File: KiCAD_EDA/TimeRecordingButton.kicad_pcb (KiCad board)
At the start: 2 copper layers, 15 x 15 mm, 9 parts, among them J1 USB Micro, J2 Battery, J3 Debug, SW1 SW_Push, U2 PIC16F18114-I/SN

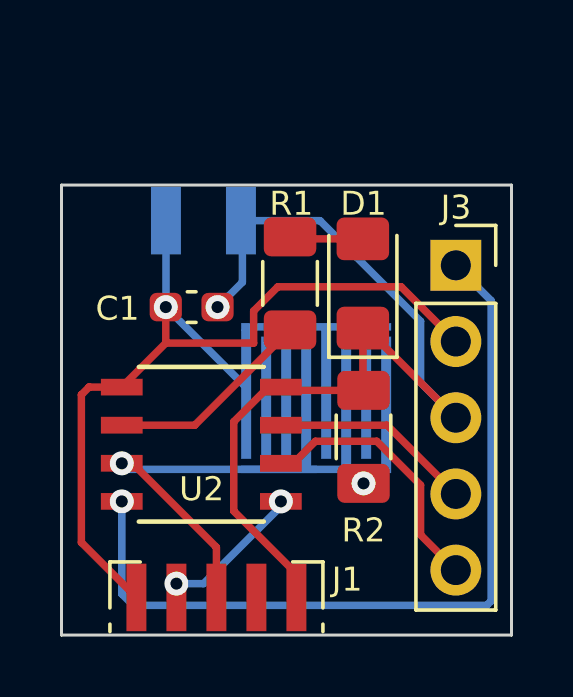
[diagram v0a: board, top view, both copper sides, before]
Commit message: KiCAD v2 and removing backup folders.
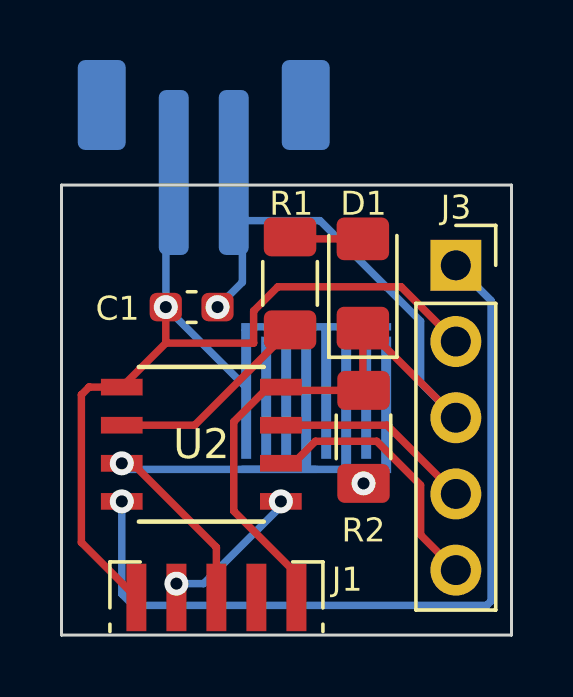
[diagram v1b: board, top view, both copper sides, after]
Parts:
- J2: footprint CustomFootprints:JST_XH_B2B-XH-A_1x02_P2.50mm_SideMount_B -> Connector_JST:JST_PH_B2B-PH-SM4-TB_1x02-1MP_P2.00mm_Vertical; moved to B.Cu
- moved J2 2.45 mm to (104.4, 101.1), turned to 180 degrees
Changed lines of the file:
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@@
     (property "ki_keywords" "PIC16F18114-I/SN")
     (attr smd)
-    (fp_text reference "U2" (at 0.008701 1.495461 unlocked) (layer "F.SilkS")
-        (effects (font (size 0.8 0.8) (thickness 0.12)))
+    (fp_text reference "U2" (at 0 0 unlocked) (layer "F.SilkS")
+        (effects (font (size 1 1) (thickness 0.15)))
     )
     (fp_text value "PIC16F18114-I/SN" (at 0 0 unlocked) (layer "F.Fab")
         (effects (font (size 1 1) (thickness 0.15)))
     )
+    (fp_text user "${REFERENCE}" (at 0 0 unlocked) (layer "F.Fab")
+        (effects (font (size 1 1) (thickness 0.15)))
+    )
+    (fp_text user "*" (at -1.5748 -2.3749) (layer "F.Fab")
+        (effects (font (size 1 1) (thickness 0.15)))
+    )
     (fp_text user "*" (at -1.5748 -2.3749 unlocked) (layer "F.Fab")
-        (effects (font (size 1 1) (thickness 0.15)))
-    )
-    (fp_text user "${REFERENCE}" (at 0 0 unlocked) (layer "F.Fab")
-        (effects (font (size 1 1) (thickness 0.15)))
-    )
-    (fp_text user "*" (at -1.5748 -2.3749) (layer "F.Fab")
         (effects (font (size 1 1) (thickness 0.15)))
     )
@@
     )
   )
-  (footprint "CustomFootprints:JST_XH_B2B-XH-A_1x02_P2.50mm_SideMount_B" (layer "F.Cu")
-    (at 103.150284 103.205284)
-    (descr "JST XH series connector, B2B-XH-A (http://www.jst-mfg.com/product/pdf/eng/eXH.pdf), generated with kicad-footprint-generator")
-    (tags "connector JST XH vertical")
-    (property "Sheetfile" "TimeRecordingButton.kicad_sch")
-    (property "Sheetname" "")
-    (property "ki_description" "Generic connector, single row, 01x02, script generated (kicad-library-utils/schlib/autogen/connector/)")
-    (property "ki_keywords" "connector")
-    (attr through_hole)
-    (fp_text reference "J2" (at -1.952554 0.834925) (layer "B.SilkS")
-        (effects (font (size 0.8 0.8) (thickness 0.12)) (justify mirror))
-    )
-    (fp_text value "Battery" (at 1.264124 -3.589534) (layer "B.Fab")
-        (effects (font (size 1 1) (thickness 0.15)))
-    )
-    (fp_text user "PCB Edge" (at 1.778593 -1.414064 180) (layer "Dwgs.User")
-        (effects (font (size 0.4 0.4) (thickness 0.04)))
-    )
-    (fp_text user "${REFERENCE}" (at 1.25 0) (layer "B.Fab")
-        (effects (font (size 1 1) (thickness 0.15)))
-    )
-    (fp_line (start -2.8 0.25) (end -2.8 1.5)
-      (stroke (width 0.12) (type solid)) (layer "B.SilkS"))
-    (fp_line (start -2.8 1.5) (end -1.55 1.5)
-      (stroke (width 0.12) (type solid)) (layer "B.SilkS"))
-    (fp_line (start -2.95 -2.85) (end -2.95 1.625)
-      (stroke (width 0.05) (type solid)) (layer "B.CrtYd"))
-    (fp_line (start -2.95 1.625) (end 5.45 1.625)
-      (stroke (width 0.05) (type solid)) (layer "B.CrtYd"))
-    (fp_line (start 5.45 -2.85) (end -2.95 -2.85)
-      (stroke (width 0.05) (type solid)) (layer "B.CrtYd"))
-    (fp_line (start 5.45 1.625) (end 5.45 -2.85)
-      (stroke (width 0.05) (type solid)) (layer "B.CrtYd"))
-    (fp_line (start -2.45 -2.35) (end -2.45 -1.125)
-      (stroke (width 0.1) (type solid)) (layer "B.Fab"))
-    (fp_line (start -2.45 -1.125) (end 4.95 -1.125)
-      (stroke (width 0.1) (type solid)) (layer "B.Fab"))
-    (fp_line (start -0.625 -2.35) (end 0 -1.35)
-      (stroke (width 0.1) (type solid)) (layer "B.Fab"))
-    (fp_line (start 0 -1.35) (end 0.625 -2.35)
-      (stroke (width 0.1) (type solid)) (layer "B.Fab"))
-    (fp_line (start 4.95 -2.35) (end -2.45 -2.35)
-      (stroke (width 0.1) (type solid)) (layer "B.Fab"))
-    (fp_line (start 4.95 -1.125) (end 4.95 -2.35)
-      (stroke (width 0.1) (type solid)) (layer "B.Fab"))
-    (pad "1" smd rect (at 0 0) (size 1 2.25) (layers "B.Cu" "B.Paste" "B.Mask")
-      (net 1 "Net-(J1-VBUS)") (pinfunction "Pin_1") (pintype "passive"))
-    (pad "2" smd rect (at 2.5 0) (size 1 2.25) (layers "B.Cu" "B.Paste" "B.Mask")
-      (net 2 "Net-(D1-K)") (pinfunction "Pin_2") (pintype "passive"))
-    (model "${KICAD6_3DMODEL_DIR}/Connector_JST.3dshapes/JST_XH_B2B-XH-A_1x02_P2.50mm_Vertical.wrl"
-      (offset (xyz 0 0 0))
-      (scale (xyz 1 1 1))
-      (rotate (xyz 0 0 0))
-    )
-  )
   (footprint "Connector_PinSocket_2.54mm:PinSocket_1x05_P2.54mm_Vertical" (layer "F.Cu")
     (at 112.812304 104.694022)
@@
       (offset (xyz 0 0 0))
       (scale (xyz 1 1 1))
+      (rotate (xyz 0 0 0))
+    )
+  )
+  (footprint "Connector_JST:JST_PH_B2B-PH-SM4-TB_1x02-1MP_P2.00mm_Vertical" (layer "B.Cu")
+    (at 104.41 101.1 180)
+    (descr "JST PH series connector, B2B-PH-SM4-TB (http://www.jst-mfg.com/product/pdf/eng/ePH.pdf), generated with kicad-footprint-generator")
+    (tags "connector JST PH side entry")
+    (property "Sheetfile" "TimeRecordingButton.kicad_sch")
+    (property "Sheetname" "")
+    (property "ki_description" "Generic connector, single row, 01x02, script generated (kicad-library-utils/schlib/autogen/connector/)")
+    (property "ki_keywords" "connector")
+    (attr smd)
+    (fp_text reference "J2" (at 0 5.45) (layer "B.SilkS")
+        (effects (font (size 1 1) (thickness 0.15)) (justify mirror))
+    )
+    (fp_text value "Battery" (at 0 -4.45) (layer "B.Fab")
+        (effects (font (size 1 1) (thickness 0.15)) (justify mirror))
+    )
+    (fp_text user "${REFERENCE}" (at 0 1) (layer "B.Fab")
+        (effects (font (size 1 1) (thickness 0.15)) (justify mirror))
+    )
+    (fp_line (start -4.085 -0.86) (end -1.76 -0.86)
+      (stroke (width 0.12) (type solid)) (layer "B.SilkS"))
+    (fp_line (start -4.085 -0.01) (end -4.085 -0.86)
+      (stroke (width 0.12) (type solid)) (layer "B.SilkS"))
+    (fp_line (start -4.085 3.51) (end -4.085 4.36)
+      (stroke (width 0.12) (type solid)) (layer "B.SilkS"))
+    (fp_line (start -4.085 4.36) (end 4.085 4.36)
+      (stroke (width 0.12) (type solid)) (layer "B.SilkS"))
+    (fp_line (start -1.76 -0.86) (end -1.76 -3.25)
+      (stroke (width 0.12) (type solid)) (layer "B.SilkS"))
+    (fp_line (start 4.085 -0.86) (end 1.76 -0.86)
+      (stroke (width 0.12) (type solid)) (layer "B.SilkS"))
+    (fp_line (start 4.085 -0.01) (end 4.085 -0.86)
+      (stroke (width 0.12) (type solid)) (layer "B.SilkS"))
+    (fp_line (start 4.085 4.36) (end 4.085 3.51)
+      (stroke (width 0.12) (type solid)) (layer "B.SilkS"))
+    (fp_line (start -4.7 -3.75) (end 4.7 -3.75)
+      (stroke (width 0.05) (type solid)) (layer "B.CrtYd"))
+    (fp_line (start -4.7 4.75) (end -4.7 -3.75)
+      (stroke (width 0.05) (type solid)) (layer "B.CrtYd"))
+    (fp_line (start 4.7 -3.75) (end 4.7 4.75)
+      (stroke (width 0.05) (type solid)) (layer "B.CrtYd"))
+    (fp_line (start 4.7 4.75) (end -4.7 4.75)
+      (stroke (width 0.05) (type solid)) (layer "B.CrtYd"))
+    (fp_line (start -3.975 -0.75) (end -3.975 4.25)
+      (stroke (width 0.1) (type solid)) (layer "B.Fab"))
+    (fp_line (start -3.975 -0.75) (end 3.975 -0.75)
+      (stroke (width 0.1) (type solid)) (layer "B.Fab"))
+    (fp_line (start -3.975 4.25) (end 3.975 4.25)
+      (stroke (width 0.1) (type solid)) (layer "B.Fab"))
+    (fp_line (start -1.5 -0.75) (end -1 -0.042893)
+      (stroke (width 0.1) (type solid)) (layer "B.Fab"))
+    (fp_line (start -1.25 2.25) (end -0.75 2.25)
+      (stroke (width 0.1) (type solid)) (layer "B.Fab"))
+    (fp_line (start -1.25 2.75) (end -1.25 2.25)
+      (stroke (width 0.1) (type solid)) (layer "B.Fab"))
+    (fp_line (start -1 -0.042893) (end -0.5 -0.75)
+      (stroke (width 0.1) (type solid)) (layer "B.Fab"))
+    (fp_line (start -0.75 2.25) (end -0.75 2.75)
+      (stroke (width 0.1) (type solid)) (layer "B.Fab"))
+    (fp_line (start -0.75 2.75) (end -1.25 2.75)
+      (stroke (width 0.1) (type solid)) (layer "B.Fab"))
+    (fp_line (start 0.75 2.25) (end 1.25 2.25)
+      (stroke (width 0.1) (type solid)) (layer "B.Fab"))
+    (fp_line (start 0.75 2.75) (end 0.75 2.25)
+      (stroke (width 0.1) (type solid)) (layer "B.Fab"))
+    (fp_line (start 1.25 2.25) (end 1.25 2.75)
+      (stroke (width 0.1) (type solid)) (layer "B.Fab"))
+    (fp_line (start 1.25 2.75) (end 0.75 2.75)
+      (stroke (width 0.1) (type solid)) (layer "B.Fab"))
+    (fp_line (start 3.975 -0.75) (end 3.975 4.25)
+      (stroke (width 0.1) (type solid)) (layer "B.Fab"))
+    (pad "1" smd roundrect (at -1 -0.5 180) (size 1 5.5) (layers "B.Cu" "B.Paste" "B.Mask") (roundrect_rratio 0.25)
+      (net 1 "Net-(J1-VBUS)") (pinfunction "Pin_1") (pintype "passive"))
+    (pad "2" smd roundrect (at 1 -0.5 180) (size 1 5.5) (layers "B.Cu" "B.Paste" "B.Mask") (roundrect_rratio 0.25)
+      (net 2 "Net-(D1-K)") (pinfunction "Pin_2") (pintype "passive"))
+    (pad "MP" smd roundrect (at -3.4 1.75 180) (size 1.6 3) (layers "B.Cu" "B.Paste" "B.Mask") (roundrect_rratio 0.15625))
+    (pad "MP" smd roundrect (at 3.4 1.75 180) (size 1.6 3) (layers "B.Cu" "B.Paste" "B.Mask") (roundrect_rratio 0.15625))
+    (model ":KICAD7_3DMODEL_DIR:Connector_JST.3dshapes/JST_PH_B2B-PH-K_1x02_P2.00mm_Vertical.step"
+      (offset (xyz 0 0 0))
+      (scale (xyz 1 1 1))
